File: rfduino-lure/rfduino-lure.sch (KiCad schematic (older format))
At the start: 4 parts

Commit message: some refactoring
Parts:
- removed U?: RFDUINO_IO, symbol RFDUINO_IO
- removed U?: RFDUINO_SHEILD, ~, symbol RFDUINO_SHEILD
- added U?: RFDUINO_IO, ~, symbol RFDUINO_IO
- added USB?: USB-PROGRAMMER, ~, symbol USB-PROGRAMMER
- gave numbers to parts that had none: 2
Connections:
- net at BLE1.1: now also U?.1 (GND)
- net at BLE1.12 (GND), U2.2 (GND): now also USB?.1 (GND)
- net at BLE1.13 (+3V), U2.4 (3V3): now also USB?.2 (+3V)
- net at BLE1.14 (RESET): now also USB?.3 (RESET)
- net at BLE1.15 (FACTORY): now also USB?.4 (FACTORY)
- net at BLE1.16 (GPIO_0/AREF), U2.17 (GPIO_UART2_TXD): now also USB?.5 (GPIO_0/AREF)
- net at BLE1.17 (GPIO_1), U2.19 (GPIO_UART2_RXD): now also USB?.6 (GPIO_1)
- net at BLE1.2 (GND): now also U?.2 (GND)
- net at BLE1.3 (GPIO_2): now also U?.3 (GPIO_2)
- net at BLE1.4 (GPIO_3): now also U?.4 (GPIO_3)
- net at BLE1.5 (GPIO_4): now also U?.5 (GPIO_4)
- net at BLE1.6 (GPIO_5): now also U?.6 (GPIO_5)
- net at BLE1.7 (GPIO_6): now also U?.7 (GPIO_6)
- net at BLE1.8 (GND): now also U?.8 (GND)
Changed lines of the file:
@@
 Sheet 1 1
 Title ""
-Date "27 mar 2015"
+Date "28 mar 2015"
 Rev ""
 Comp ""
@@
 $EndDescr
 $Comp
-L RFDUINO BLE?
+L RFDUINO BLE1
 U 1 1 5515110B
 P 1200 3800
-F 0 "BLE?" H 1200 3200 60  0000 C CNN
+F 0 "BLE1" H 1200 3200 60  0000 C CNN
 F 1 "RFDUINO" H 1200 4500 60  0000 C CNN
 F 2 "~" H 1200 3800 60  0000 C CNN
@@
 $EndComp
 $Comp
-L MAX_LSE U?
+L MAX_LSE U2
 U 1 1 5515147E
 P 3550 5950
-F 0 "U?" H 3550 5300 60  0000 C CNN
+F 0 "U2" H 3550 5300 60  0000 C CNN
 F 1 "MAX_LSE" H 3650 7550 60  0000 C CNN
 F 2 "~" H 4250 6000 60  0000 C CNN
@@
 	1    3550 5950
 	-1   0    0    1
-$EndComp
-$Comp
-L RFDUINO_IO U?
-U 1 1 551519C4
-P 4100 3000
-F 0 "U?" H 4100 3000 60  0000 C CNN
-F 1 "RFDUINO_IO" H 4100 4050 60  0000 C CNN
-F 2 "" H 4100 3000 60  0000 C CNN
-F 3 "" H 4100 3000 60  0000 C CNN
-	1    4100 3000
-	1    0    0    -1
-$EndComp
-$Comp
-L RFDUINO_SHEILD U?
-U 1 1 55152170
-P 3300 3900
-F 0 "U?" H 3300 3900 60  0000 C CNN
-F 1 "RFDUINO_SHEILD" H 3300 4950 60  0000 C CNN
-F 2 "~" H 3300 3900 60  0000 C CNN
-F 3 "~" H 3300 3900 60  0000 C CNN
-	1    3300 3900
-	0    -1   -1   0
 $EndComp
 Wire Wire Line
@@
 Connection ~ 1200 6450
 Wire Wire Line
-	3700 2200 1100 2200
-Wire Wire Line
-	1100 2200 1100 3050
-Wire Wire Line
 	1200 3050 1200 2300
-Wire Wire Line
-	1200 2300 3700 2300
 Wire Wire Line
 	1300 3050 1300 2400
 Wire Wire Line
-	1300 2400 3700 2400
-Wire Wire Line
 	1400 3050 1400 2500
-Wire Wire Line
-	1400 2500 3700 2500
-Wire Wire Line
-	3700 2600 1500 2600
 Wire Wire Line
 	1500 2600 1500 3050
 Wire Wire Line
 	1600 3050 1600 2700
-Wire Wire Line
-	1600 2700 3700 2700
-Wire Wire Line
-	3700 2800 1700 2800
-Wire Wire Line
-	1700 2800 1700 3050
-Wire Wire Line
-	1800 3050 1800 2900
-Wire Wire Line
-	1800 2900 3700 2900
-Wire Wire Line
-	2550 3100 2550 2300
-Connection ~ 2550 2300
-Wire Wire Line
-	2650 3100 2650 2400
-Connection ~ 2650 2400
-Wire Wire Line
-	2750 3100 2750 2500
-Connection ~ 2750 2500
-Wire Wire Line
-	2850 3100 2850 2600
-Connection ~ 2850 2600
-Wire Wire Line
-	2950 3100 2950 2700
-Connection ~ 2950 2700
 Wire Wire Line
 	2850 4600 2850 4950
@@
 Wire Wire Line
 	2450 6300 1100 6300
+$Comp
+L USB-PROGRAMMER USB?
+U 1 1 55163475
+P 2600 4200
+F 0 "USB?" H 2650 3650 60  0000 C CNN
+F 1 "USB-PROGRAMMER" H 2600 4500 60  0000 C CNN
+F 2 "~" H 2600 4200 60  0000 C CNN
+F 3 "~" H 2600 4200 60  0000 C CNN
+	1    2600 4200
+	0    -1   -1   0
+$EndComp
+$Comp
+L RFDUINO_IO U?
+U 1 1 5516349D
+P 2950 3000
+F 0 "U?" H 2950 3000 60  0000 C CNN
+F 1 "RFDUINO_IO" H 2950 4050 60  0000 C CNN
+F 2 "~" H 2950 3000 60  0000 C CNN
+F 3 "~" H 2950 3000 60  0000 C CNN
+	1    2950 3000
+	1    0    0    -1
+$EndComp
+Wire Wire Line
+	1600 2700 2550 2700
+Wire Wire Line
+	2550 2800 1700 2800
+Wire Wire Line
+	1700 2800 1700 3050
+Wire Wire Line
+	2550 2900 1800 2900
+Wire Wire Line
+	1800 2900 1800 3050
+Wire Wire Line
+	1100 3050 1100 2200
+Wire Wire Line
+	1100 2200 2550 2200
+Wire Wire Line
+	1400 2500 2550 2500
+Wire Wire Line
+	2550 2600 1500 2600
+Wire Wire Line
+	1300 2400 2550 2400
+Wire Wire Line
+	1200 2300 2550 2300
 $EndSCHEMATC

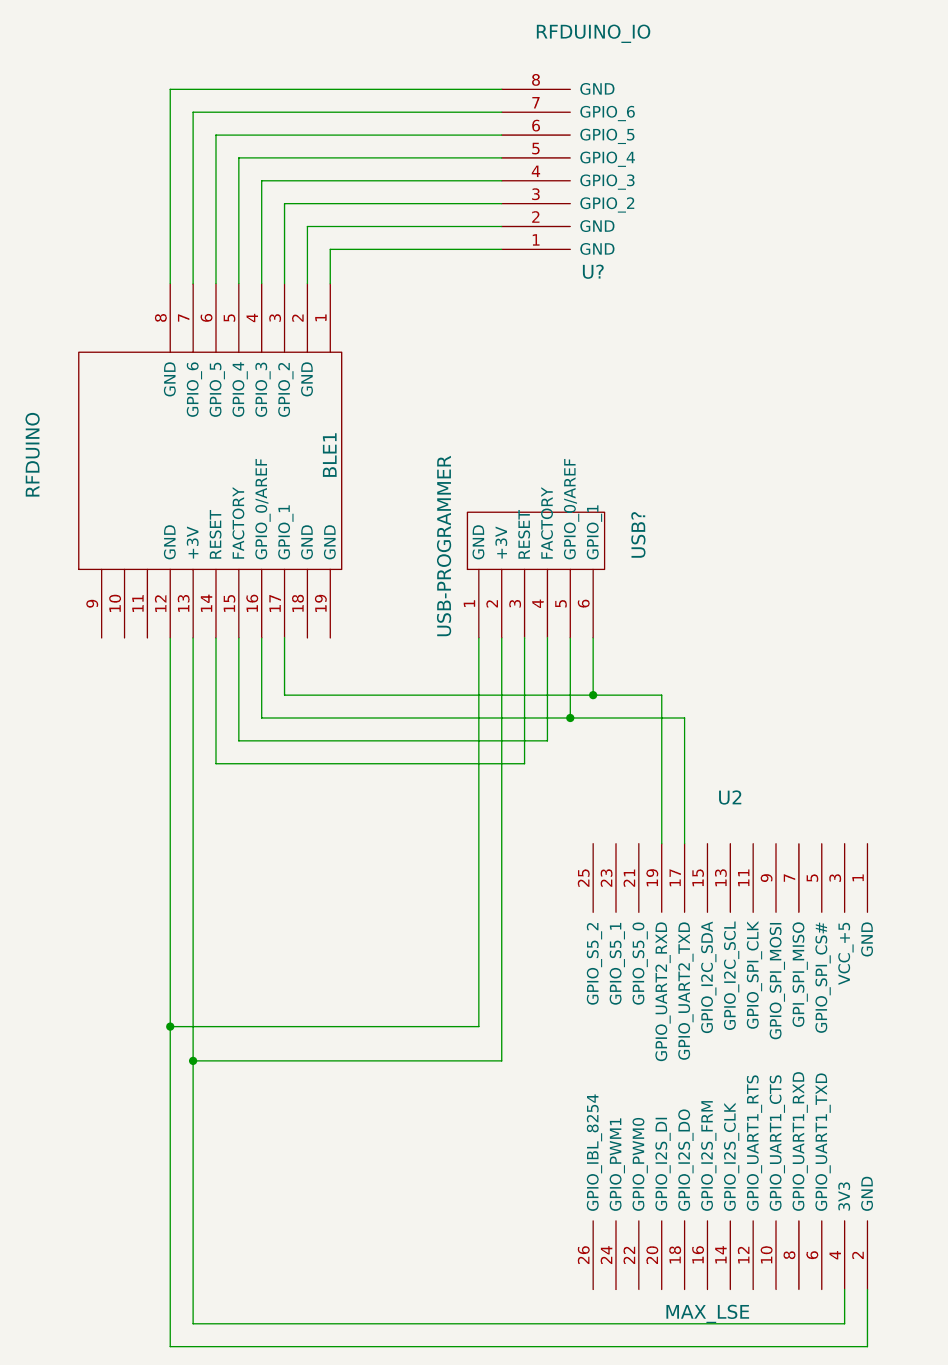
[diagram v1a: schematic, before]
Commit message: added ground plane
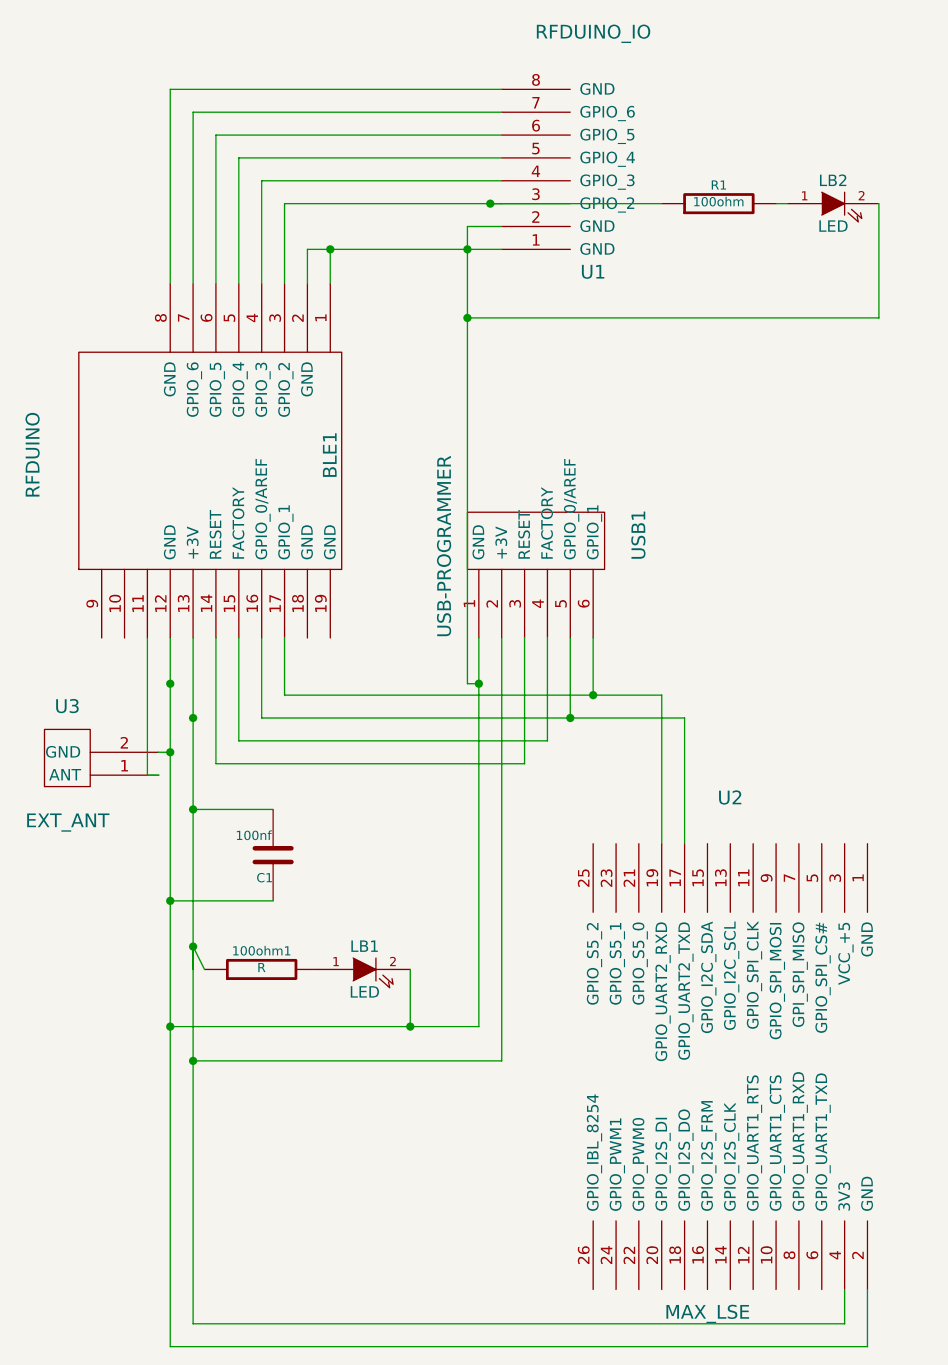
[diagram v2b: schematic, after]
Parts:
- added 100ohm1: R, ~, symbol R
- added C1: 100nf, ~, symbol C
- added LB1, LB2: LED, ~, symbol LED
- added R1: 100ohm, ~, symbol R
- added U3: EXT_ANT, symbol EXT_ANT
- gave numbers to parts that had none: 2
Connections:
- net at BLE1.1, U1.1 (GND): now also BLE1.12 (GND), BLE1.2 (GND), U1.2 (GND), U2.2 (GND), USB1.1 (GND), C1.1, LB1.2 (K), LB2.2 (K), U3.2 (GND)
- net at BLE1.11: now also U3.1 (ANT)
- net at BLE1.13 (+3V), U2.4 (3V3), USB1.2 (+3V): now also 100ohm1.1, C1.2
- net at BLE1.3 (GPIO_2), U1.3 (GPIO_2): now also R1.1
- new net: LB2.1 (A), R1.2
- new net: 100ohm1.2, LB1.1 (A)
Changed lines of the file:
@@
 LIBS:contrib
 LIBS:valves
-LIBS:blelight
 LIBS:max_lse
 LIBS:rfduino_sheild
@@
 Sheet 1 1
 Title ""
-Date "28 mar 2015"
+Date "6 apr 2015"
 Rev ""
 Comp ""
@@
 	-1   0    0    1
 $EndComp
-Wire Wire Line
-	1200 4600 1200 7600
-Wire Wire Line
-	1200 7600 4050 7600
-Wire Wire Line
-	4050 7600 4050 7450
-Wire Wire Line
-	1100 4600 1100 7700
-Wire Wire Line
-	1100 7700 4150 7700
-Wire Wire Line
-	4150 7700 4150 7450
-Wire Wire Line
-	3250 4850 3250 5500
-Wire Wire Line
-	1600 4850 3250 4850
-Wire Wire Line
-	1600 4850 1600 4600
-Wire Wire Line
-	3350 4950 3350 5500
-Wire Wire Line
-	1500 4950 3350 4950
-Wire Wire Line
-	1500 4950 1500 4600
-Connection ~ 1100 6300
-Connection ~ 1200 6450
-Wire Wire Line
-	1200 3050 1200 2300
-Wire Wire Line
-	1300 3050 1300 2400
-Wire Wire Line
-	1400 3050 1400 2500
-Wire Wire Line
-	1500 2600 1500 3050
-Wire Wire Line
-	1600 3050 1600 2700
-Wire Wire Line
-	2850 4600 2850 4950
-Connection ~ 2850 4950
-Wire Wire Line
-	2950 4600 2950 4850
-Connection ~ 2950 4850
-Wire Wire Line
-	2750 4600 2750 5050
-Wire Wire Line
-	2750 5050 1400 5050
-Wire Wire Line
-	1400 5050 1400 4600
-Wire Wire Line
-	2650 4600 2650 5150
-Wire Wire Line
-	2650 5150 1300 5150
-Wire Wire Line
-	1300 5150 1300 4600
-Wire Wire Line
-	2550 4600 2550 6450
-Wire Wire Line
-	2550 6450 1200 6450
-Wire Wire Line
-	2450 4600 2450 6300
-Wire Wire Line
-	2450 6300 1100 6300
-$Comp
-L USB-PROGRAMMER USB?
+$Comp
+L USB-PROGRAMMER USB1
 U 1 1 55163475
 P 2600 4200
-F 0 "USB?" H 2650 3650 60  0000 C CNN
+F 0 "USB1" H 2650 3650 60  0000 C CNN
 F 1 "USB-PROGRAMMER" H 2600 4500 60  0000 C CNN
 F 2 "~" H 2600 4200 60  0000 C CNN
@@
 $EndComp
 $Comp
-L RFDUINO_IO U?
+L RFDUINO_IO U1
 U 1 1 5516349D
 P 2950 3000
-F 0 "U?" H 2950 3000 60  0000 C CNN
+F 0 "U1" H 2950 3000 60  0000 C CNN
 F 1 "RFDUINO_IO" H 2950 4050 60  0000 C CNN
 F 2 "~" H 2950 3000 60  0000 C CNN
@@
 $EndComp
 Wire Wire Line
+	1200 4600 1200 6050
+Wire Wire Line
+	1200 5950 1200 7600
+Wire Wire Line
+	1200 7600 4050 7600
+Wire Wire Line
+	4050 7600 4050 7450
+Wire Wire Line
+	1100 4600 1100 7700
+Wire Wire Line
+	1100 7700 4150 7700
+Wire Wire Line
+	4150 7700 4150 7450
+Wire Wire Line
+	3250 4850 3250 5500
+Wire Wire Line
+	1600 4850 3250 4850
+Wire Wire Line
+	1600 4850 1600 4600
+Wire Wire Line
+	3350 4950 3350 5500
+Wire Wire Line
+	1500 4950 3350 4950
+Wire Wire Line
+	1500 4950 1500 4600
+Connection ~ 1100 6300
+Connection ~ 1200 6450
+Wire Wire Line
+	1200 3050 1200 2300
+Wire Wire Line
+	1300 3050 1300 2400
+Wire Wire Line
+	1400 3050 1400 2500
+Wire Wire Line
+	1500 2600 1500 3050
+Wire Wire Line
+	1600 3050 1600 2700
+Wire Wire Line
+	2850 4600 2850 4950
+Connection ~ 2850 4950
+Wire Wire Line
+	2950 4600 2950 4850
+Connection ~ 2950 4850
+Wire Wire Line
+	2750 4600 2750 5050
+Wire Wire Line
+	2750 5050 1400 5050
+Wire Wire Line
+	1400 5050 1400 4600
+Wire Wire Line
+	2650 4600 2650 5150
+Wire Wire Line
+	2650 5150 1300 5150
+Wire Wire Line
+	1300 5150 1300 4600
+Wire Wire Line
+	2550 4600 2550 6450
+Wire Wire Line
+	2550 6450 1200 6450
+Wire Wire Line
+	2450 6300 2450 4600
+Wire Wire Line
+	1100 6300 2450 6300
+Wire Wire Line
 	1600 2700 2550 2700
 Wire Wire Line
-	2550 2800 1700 2800
-Wire Wire Line
-	1700 2800 1700 3050
-Wire Wire Line
-	2550 2900 1800 2900
+	1100 3050 1100 2200
+Wire Wire Line
+	1100 2200 2550 2200
+Wire Wire Line
+	1400 2500 2550 2500
+Wire Wire Line
+	2550 2600 1500 2600
+Wire Wire Line
+	1300 2400 2550 2400
+Wire Wire Line
+	1200 2300 2550 2300
+Wire Wire Line
+	2550 2800 2400 2800
+Wire Wire Line
+	2400 2800 2400 4800
+Wire Wire Line
+	2400 4800 2450 4800
+Connection ~ 2450 4800
+Wire Wire Line
+	1700 2900 2550 2900
+Connection ~ 2400 2900
 Wire Wire Line
 	1800 2900 1800 3050
 Wire Wire Line
-	1100 3050 1100 2200
-Wire Wire Line
-	1100 2200 2550 2200
-Wire Wire Line
-	1400 2500 2550 2500
-Wire Wire Line
-	2550 2600 1500 2600
-Wire Wire Line
-	1300 2400 2550 2400
-Wire Wire Line
-	1200 2300 2550 2300
+	1700 2900 1700 3050
+Connection ~ 1800 2900
+$Comp
+L C C1
+U 1 1 5522B758
+P 1550 5550
+F 0 "C1" H 1550 5650 40  0000 L CNN
+F 1 "100nf" H 1556 5465 40  0000 L CNN
+F 2 "~" H 1588 5400 30  0000 C CNN
+F 3 "~" H 1550 5550 60  0000 C CNN
+	1    1550 5550
+	-1   0    0    1
+$EndComp
+Connection ~ 1200 4950
+Connection ~ 1100 4800
+$Comp
+L LED LB2
+U 1 1 5522C4E7
+P 4000 2700
+F 0 "LB2" H 4000 2800 50  0000 C CNN
+F 1 "LED" H 4000 2600 50  0000 C CNN
+F 2 "~" H 4000 2700 60  0000 C CNN
+F 3 "~" H 4000 2700 60  0000 C CNN
+	1    4000 2700
+	1    0    0    -1
+$EndComp
+Wire Wire Line
+	1550 5350 1200 5350
+Connection ~ 1200 5350
+Wire Wire Line
+	1550 5750 1100 5750
+Connection ~ 1100 5750
+$Comp
+L EXT_ANT U3
+U 1 1 5522C879
+P 650 5150
+F 0 "U3" H 650 4900 60  0000 C CNN
+F 1 "EXT_ANT" H 650 5400 60  0000 C CNN
+F 2 "" H 650 4750 60  0000 C CNN
+F 3 "" H 650 4750 60  0000 C CNN
+	1    650  5150
+	-1   0    0    1
+$EndComp
+Wire Wire Line
+	1050 5100 1100 5100
+Connection ~ 1100 5100
+Wire Wire Line
+	1000 4600 1000 5200
+Wire Wire Line
+	1000 5200 1050 5200
+Connection ~ 2500 2700
+Wire Wire Line
+	4200 2700 4200 3200
+Wire Wire Line
+	4200 3200 2400 3200
+Connection ~ 2400 3200
+$Comp
+L LED LB1
+U 1 1 5522CACA
+P 1950 6050
+F 0 "LB1" H 1950 6150 50  0000 C CNN
+F 1 "LED" H 1950 5950 50  0000 C CNN
+F 2 "~" H 1950 6050 60  0000 C CNN
+F 3 "~" H 1950 6050 60  0000 C CNN
+	1    1950 6050
+	1    0    0    -1
+$EndComp
+$Comp
+L R 100ohm1
+U 1 1 5522CB61
+P 1500 6050
+F 0 "100ohm1" V 1580 6050 40  0000 C CNN
+F 1 "R" V 1507 6051 40  0000 C CNN
+F 2 "~" V 1430 6050 30  0000 C CNN
+F 3 "~" H 1500 6050 30  0000 C CNN
+	1    1500 6050
+	0    -1   -1   0
+$EndComp
+Wire Wire Line
+	1750 6050 1750 6050
+Wire Wire Line
+	2150 6050 2150 6300
+Connection ~ 2150 6300
+Wire Wire Line
+	1250 6050 1200 5950
+Connection ~ 1200 5950
+$Comp
+L R R1
+U 1 1 5522CC46
+P 3500 2700
+F 0 "R1" V 3580 2700 40  0000 C CNN
+F 1 "100ohm" V 3507 2701 40  0000 C CNN
+F 2 "~" V 3430 2700 30  0000 C CNN
+F 3 "~" H 3500 2700 30  0000 C CNN
+	1    3500 2700
+	0    -1   -1   0
+$EndComp
+Wire Wire Line
+	2500 2700 3250 2700
+Wire Wire Line
+	3800 2700 3750 2700
 $EndSCHEMATC
